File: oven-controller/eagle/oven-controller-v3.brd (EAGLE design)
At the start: 74.3 x 45.4 mm, 48 parts, among them Q1 FDV305N, Q2 FDV305N, Q3 FDV305N, Q4 FDV305N, U1 ARDUINO_SHIELDLONGPADS, U2 MAX31855, U3 MAX31855, U4 MAX31855, U5 MAX31855, U6 MAX31855

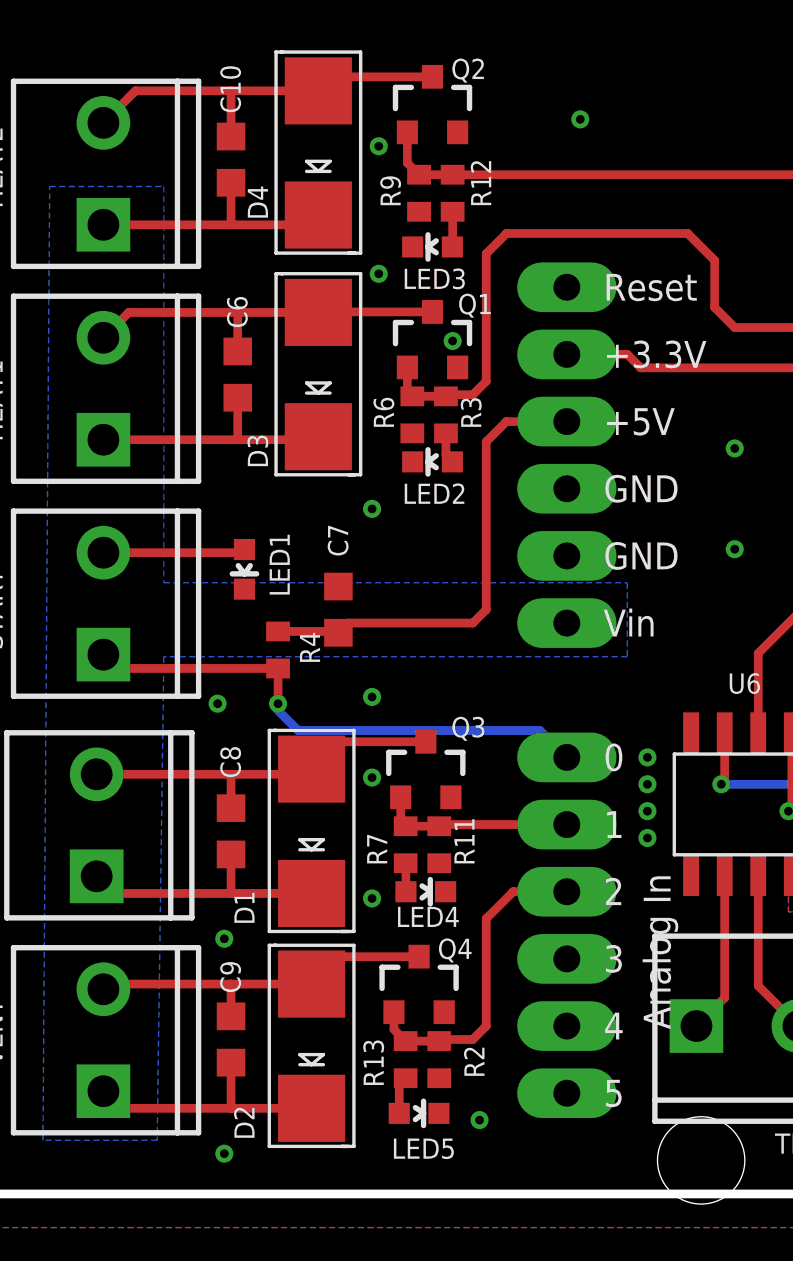
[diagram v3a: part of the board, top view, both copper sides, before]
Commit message: Added BOM.
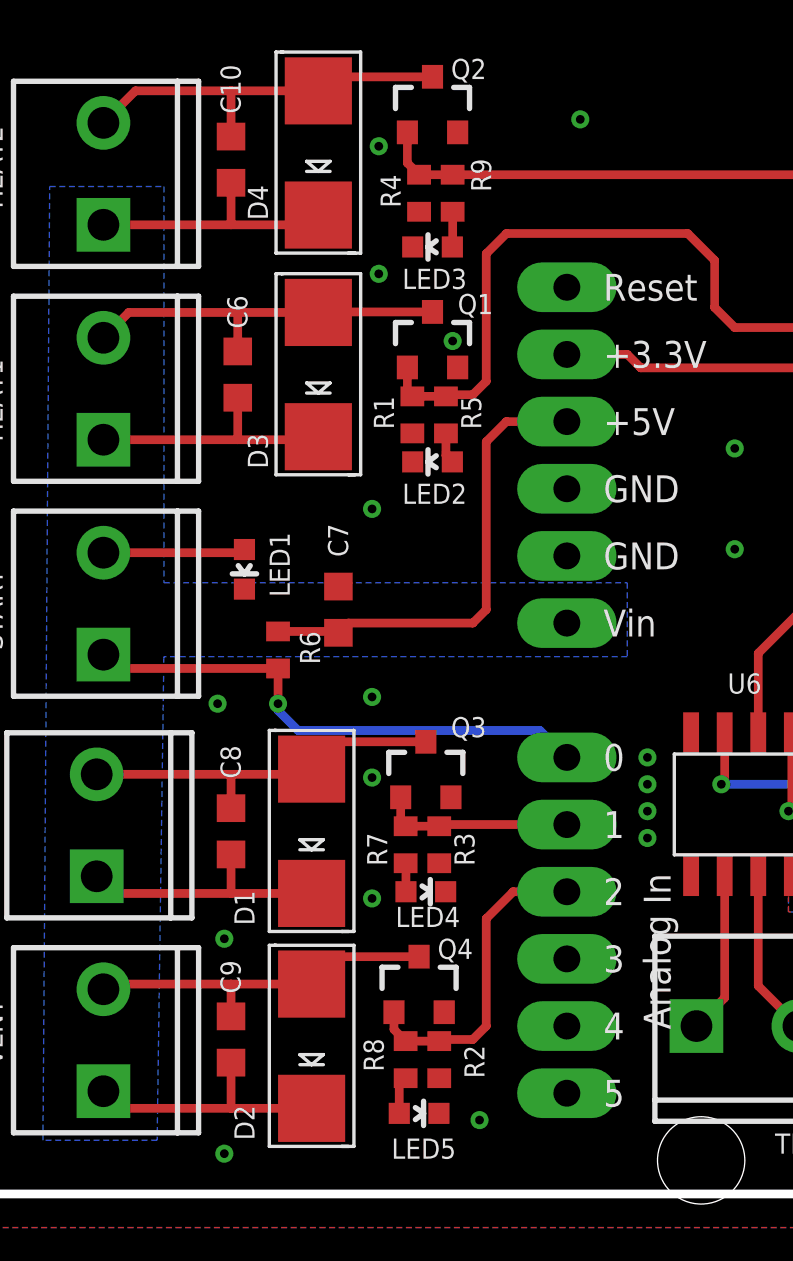
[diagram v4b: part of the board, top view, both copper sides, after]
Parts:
- removed R11: 10k, rcl_custom:0603-C-NOSILK
- removed R12: 330, rcl_custom:0603-C-NOSILK
- added R1: 10k, rcl_custom:0603-C-NOSILK
- added R5: 330, rcl_custom:0603-C-NOSILK
- R3, R4: value 330 -> 10k
- R6, R9: value 10k -> 330
- moved R4 18.1 mm to (15.0, 36.6)
- moved R3 16.3 mm to (15.7, 11.9)
- moved R6 10.2 mm to (9.65, 19.3)
- moved R9 1.27 mm to (16.3, 36.6)
- renumbered R13 to R8
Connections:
- net 5V: now also R6.2; no longer R4.2
- net CS_FAN: now also R3.2; no longer R11.2
- net CS_HEAT1: now also R1.2, R5.2; no longer R3.2, R6.2
- net CS_HEAT2: now also R4.2; no longer R12.2
- net GND: now also R1.1, R3.1, R4.1; no longer R11.1, R6.1, R9.1
- net N$18: now also R9.1; no longer R12.1
- net N$7: now also R5.1; no longer R3.1
- net START: now also R6.1; no longer R4.1
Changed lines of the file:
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@@
 <attribute name="VALUE" x="17.748" y="3.01" size="1" layer="27" ratio="10" rot="R90"/>
 </element>
-<element name="R4" library="rcl_custom" package="0603-C-NOSILK" value="330" x="9.652" y="19.304" smashed="yes" rot="R90">
+<element name="R6" library="rcl_custom" package="0603-C-NOSILK" value="330" x="9.652" y="19.304" smashed="yes" rot="R90">
 <attribute name="NAME" x="11.242" y="18.758" size="0.762" layer="25" font="vector" ratio="20" rot="R90"/>
 <attribute name="VALUE" x="11.652" y="18.504" size="1" layer="27" ratio="10" rot="R90"/>
@@
 <attribute name="VALUE" x="16.51" y="27.4955" size="0.4064" layer="27" rot="R180"/>
 </element>
-<element name="R3" library="rcl_custom" package="0603-C-NOSILK" value="330" x="16.002" y="28.194" smashed="yes" rot="R90">
+<element name="R5" library="rcl_custom" package="0603-C-NOSILK" value="330" x="16.002" y="28.194" smashed="yes" rot="R90">
 <attribute name="NAME" x="17.338" y="27.648" size="0.762" layer="25" font="vector" ratio="10" rot="R90"/>
 <attribute name="VALUE" x="18.002" y="27.394" size="1" layer="27" ratio="10" rot="R90"/>
@@
 <attribute name="VALUE" x="14.478" y="30.7975" size="0.4064" layer="27"/>
 </element>
-<element name="R6" library="rcl_custom" package="0603-C-NOSILK" value="10k" x="14.732" y="28.194" smashed="yes" rot="R90">
+<element name="R1" library="rcl_custom" package="0603-C-NOSILK" value="10k" x="14.732" y="28.194" smashed="yes" rot="R90">
 <attribute name="NAME" x="14.036" y="27.648" size="0.762" layer="25" font="vector" ratio="20" rot="R90"/>
 <attribute name="VALUE" x="16.732" y="27.394" size="1" layer="27" ratio="10" rot="R90"/>
@@
 <attribute name="VALUE" x="14.478" y="39.6875" size="0.4064" layer="27"/>
 </element>
-<element name="R9" library="rcl_custom" package="0603-C-NOSILK" value="10k" x="14.986" y="36.576" smashed="yes" rot="R90">
+<element name="R4" library="rcl_custom" package="0603-C-NOSILK" value="10k" x="14.986" y="36.576" smashed="yes" rot="R90">
 <attribute name="NAME" x="14.29" y="36.03" size="0.762" layer="25" font="vector" ratio="20" rot="R90"/>
 <attribute name="VALUE" x="16.986" y="35.776" size="1" layer="27" ratio="10" rot="R90"/>
@@
 <attribute name="VALUE" x="14.224" y="14.5415" size="0.4064" layer="27"/>
 </element>
-<element name="R11" library="rcl_custom" package="0603-C-NOSILK" value="10k" x="15.748" y="11.938" smashed="yes" rot="R90">
+<element name="R3" library="rcl_custom" package="0603-C-NOSILK" value="10k" x="15.748" y="11.938" smashed="yes" rot="R90">
 <attribute name="NAME" x="17.084" y="11.138" size="0.762" layer="25" font="vector" ratio="10" rot="R90"/>
 <attribute name="VALUE" x="17.748" y="11.138" size="1" layer="27" ratio="10" rot="R90"/>
@@
 <attribute name="VALUE" x="16.51" y="35.6235" size="0.4064" layer="27" rot="R180"/>
 </element>
-<element name="R12" library="rcl_custom" package="0603-C-NOSILK" value="330" x="16.256" y="36.576" smashed="yes" rot="R90">
+<element name="R9" library="rcl_custom" package="0603-C-NOSILK" value="330" x="16.256" y="36.576" smashed="yes" rot="R90">
 <attribute name="NAME" x="16.952" y="37.884" size="0.762" layer="25" font="vector" ratio="10" rot="R270"/>
 <attribute name="VALUE" x="18.256" y="35.776" size="1" layer="27" ratio="10" rot="R90"/>
@@
 <attribute name="VALUE" x="13.97" y="0.6985" size="0.4064" layer="27"/>
 </element>
-<element name="R13" library="rcl_custom" package="0603-C-NOSILK" value="330" x="14.478" y="3.81" smashed="yes" rot="R90">
+<element name="R8" library="rcl_custom" package="0603-C-NOSILK" value="330" x="14.478" y="3.81" smashed="yes" rot="R90">
 <attribute name="NAME" x="12.888" y="4.61" size="0.762" layer="25" font="vector" ratio="20" rot="R270"/>
 <attribute name="VALUE" x="16.478" y="3.01" size="1" layer="27" ratio="10" rot="R90"/>
@@
 <vertex x="-3.302" y="45.72"/>
 </polygon>
-<contactref element="R9" pad="1"/>
+<contactref element="R4" pad="1"/>
 <contactref element="LED3" pad="C"/>
-<contactref element="R6" pad="1"/>
+<contactref element="R1" pad="1"/>
 <contactref element="Q1" pad="2"/>
 <contactref element="LED2" pad="C"/>
 <contactref element="LED5" pad="C"/>
 <contactref element="R2" pad="1"/>
-<contactref element="R11" pad="1"/>
+<contactref element="R3" pad="1"/>
 <contactref element="LED4" pad="C"/>
 <polygon width="0.3302" layer="1" isolate="0.508" rank="6">
@@
 <contactref element="START" pad="1"/>
 <contactref element="U1" pad="A0"/>
-<contactref element="R4" pad="1"/>
+<contactref element="R6" pad="1"/>
 <wire x1="9.652" y1="18.604" x2="3.5702" y2="18.604" width="0.3302" layer="1"/>
 <wire x1="3.5702" y1="18.604" x2="3.048" y2="19.1262" width="0.3302" layer="1"/>
@@
 </signal>
 <signal name="5V">
-<contactref element="R4" pad="2"/>
+<contactref element="R6" pad="2"/>
 <contactref element="U1" pad="5V"/>
 <contactref element="C7" pad="1"/>
@@
 <signal name="N$7">
 <contactref element="LED2" pad="A"/>
-<contactref element="R3" pad="1"/>
+<contactref element="R5" pad="1"/>
 <wire x1="16.002" y1="27.494" x2="16.002" y2="26.658" width="0.3302" layer="1"/>
 <wire x1="16.002" y1="26.658" x2="16.244" y2="26.416" width="0.3302" layer="1"/>
@@
 </signal>
 <signal name="CS_VENT">
-<contactref element="R13" pad="2"/>
+<contactref element="R8" pad="2"/>
 <contactref element="U1" pad="A2"/>
 <contactref element="Q4" pad="1"/>
@@
 </signal>
 <signal name="CS_HEAT1">
-<contactref element="R3" pad="2"/>
+<contactref element="R5" pad="2"/>
 <contactref element="U1" pad="D5"/>
 <wire x1="64.516" y1="17.018" x2="66.04" y2="15.24" width="0.3302" layer="16"/>
 <wire x1="66.04" y1="15.24" x2="68.834" y2="15.24" width="0.3302" layer="16"/>
 <contactref element="Q1" pad="1"/>
-<contactref element="R6" pad="2"/>
+<contactref element="R1" pad="2"/>
 <wire x1="14.544" y1="29.988" x2="14.544" y2="29.082" width="0.3302" layer="1"/>
 <wire x1="14.544" y1="29.082" x2="14.732" y2="28.894" width="0.3302" layer="1"/>
@@
 </signal>
 <signal name="CS_HEAT2">
-<contactref element="R12" pad="2"/>
+<contactref element="R9" pad="2"/>
 <contactref element="U1" pad="D6"/>
-<contactref element="R9" pad="2"/>
+<contactref element="R4" pad="2"/>
 <contactref element="Q2" pad="1"/>
 <wire x1="14.544" y1="38.878" x2="14.544" y2="37.718" width="0.3302" layer="1"/>
@@
 <contactref element="R7" pad="2"/>
 <contactref element="U1" pad="A1"/>
-<contactref element="R11" pad="2"/>
+<contactref element="R3" pad="2"/>
 <contactref element="Q3" pad="1"/>
 <wire x1="14.29" y1="13.732" x2="14.29" y2="12.826" width="0.3302" layer="1"/>
@@
 <signal name="N$18">
 <contactref element="LED3" pad="A"/>
-<contactref element="R12" pad="1"/>
+<contactref element="R9" pad="1"/>
 <wire x1="16.256" y1="35.876" x2="16.256" y2="34.556" width="0.3302" layer="1"/>
 <wire x1="16.256" y1="34.556" x2="16.244" y2="34.544" width="0.3302" layer="1"/>
@@
 <signal name="N$19">
 <contactref element="LED5" pad="A"/>
-<contactref element="R13" pad="1"/>
+<contactref element="R8" pad="1"/>
 <wire x1="14.236" y1="1.778" x2="14.236" y2="2.868" width="0.3302" layer="1"/>
 <wire x1="14.236" y1="2.868" x2="14.478" y2="3.11" width="0.3302" layer="1"/>
